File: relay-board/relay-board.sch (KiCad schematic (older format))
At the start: 74 parts, among them IC1 LTV-357T, IC2 LTV-357T, IC3 LTV-357T, IC4 LTV-357T, IC5 LTV-357T, IC6 LTV-357T, IC7 LTV-357T, IC8 LTV-357T, K1 RELAY_JS5N-K, K10 CONN_3, K11 CONN_3, K12 CONN_3, K13 CONN_3, K14 CONN_3, K15 CONN_3, K16 CONN_3, K2 RELAY_JS5N-K, K3 RELAY_JS5N-K, K4 RELAY_JS5N-K, K5 RELAY_JS5N-K, K6 RELAY_JS5N-K, K7 RELAY_JS5N-K, K8 RELAY_JS5N-K, K9 CONN_3, P1 CONN_4, P2 CONN_4, P3 DIL6, P4 CONN_2, P5 CONN_2, Q1 BS107, Q2 BS107, Q3 BS107, Q4 BS107, Q5 BS107, Q6 BS107, Q7 BS107, Q8 BS107, U1 PCF8574

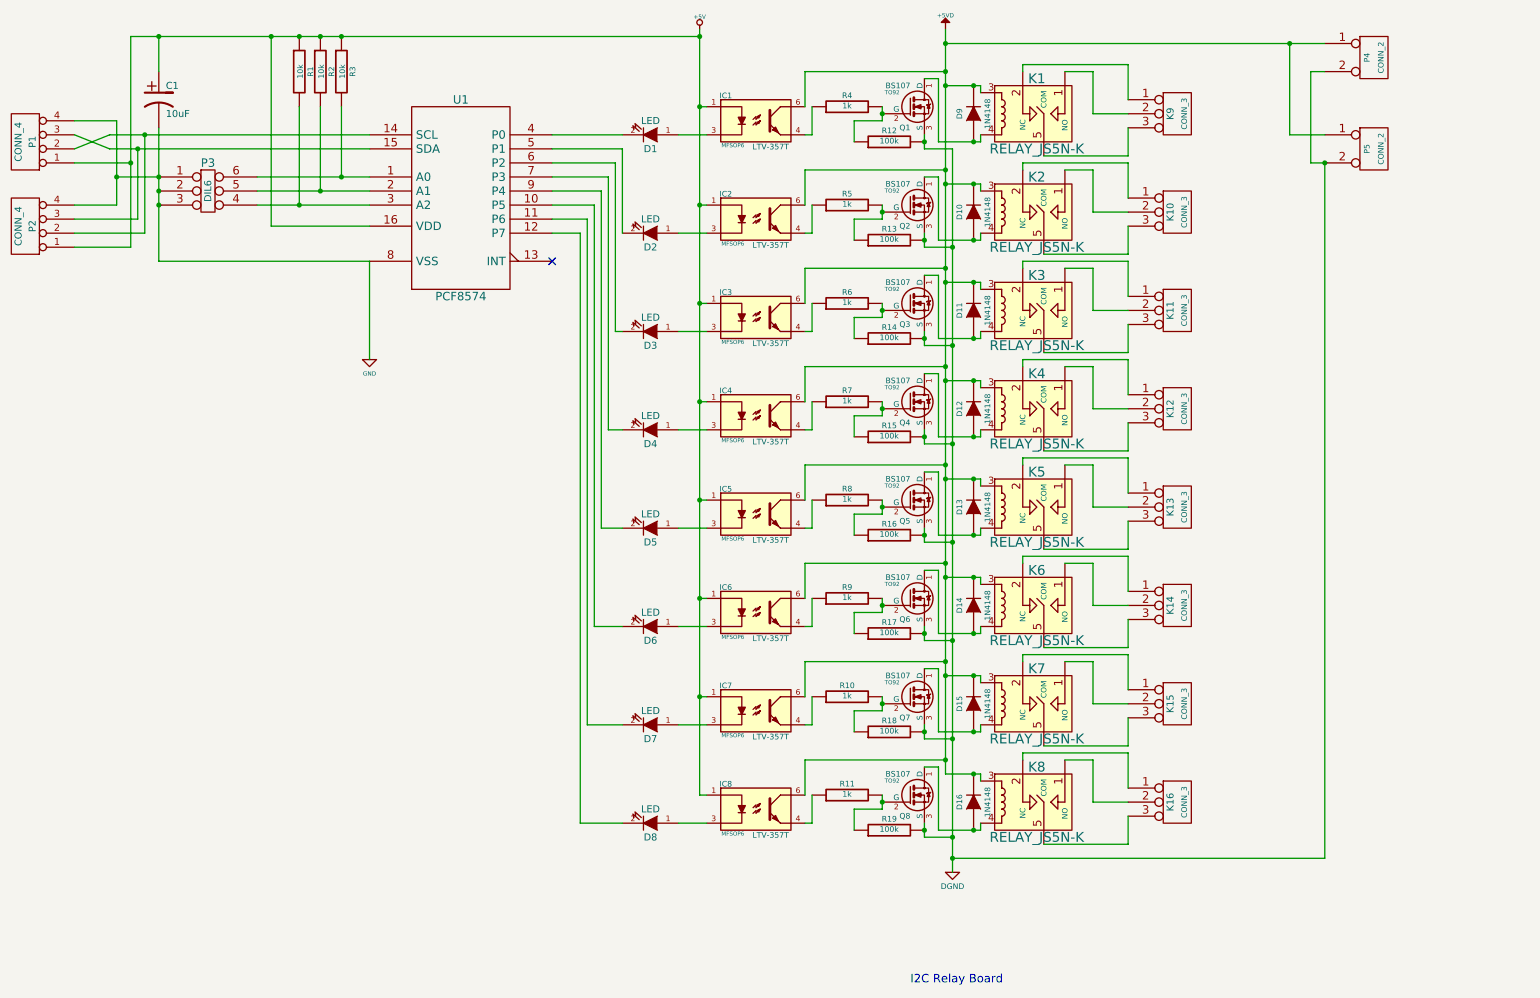
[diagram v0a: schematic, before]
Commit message: [relay-board] Updated schema, created PCB and added libraries with modules.
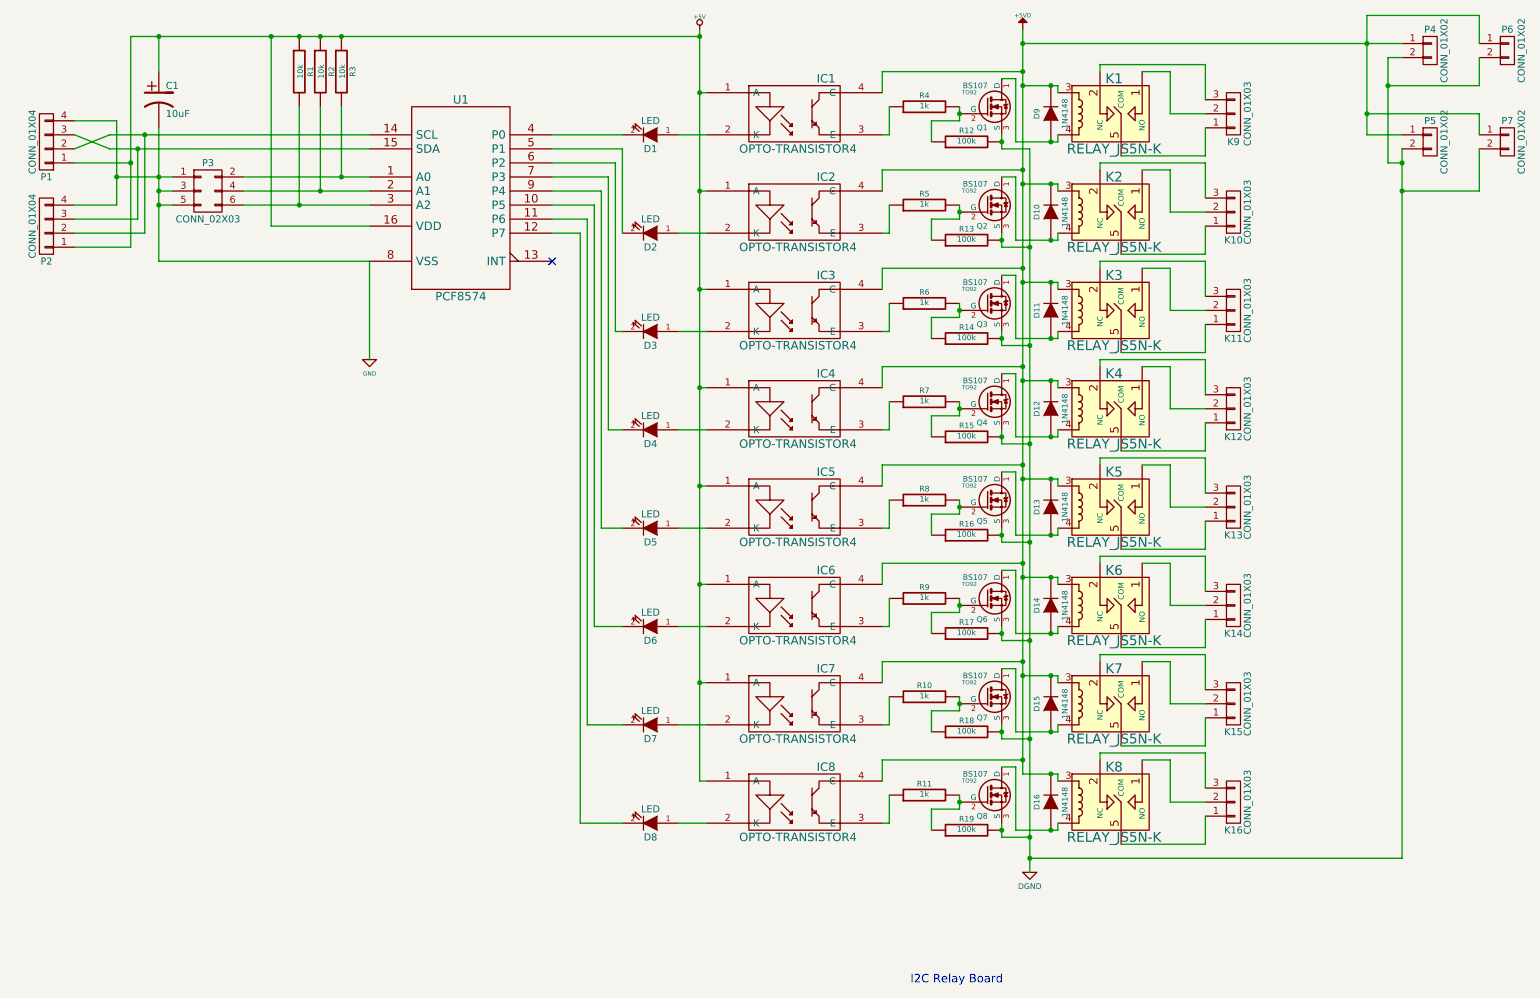
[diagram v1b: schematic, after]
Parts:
- removed IC1, IC2, IC3, IC4, IC5, IC6, IC7, IC8: LTV-357T, MFSOP6, symbol LTV-357T
- removed K10, K11, K12, K13, K14, K15, K16, K9: CONN_3, ~, symbol CONN_3
- removed P1, P2: CONN_4, ~, symbol CONN_4
- removed P3: DIL6, ~, symbol DIL6
- removed P4, P5: CONN_2, ~, symbol CONN_2
- added IC1, IC2, IC3, IC4, IC5, IC6, IC7, IC8: OPTO-TRANSISTOR4, symbol OPTO-TRANSISTOR4
- added K10, K11, K12, K13, K14, K15, K16, K9: CONN_01X03, symbol CONN_01X03
- added P1, P2: CONN_01X04, symbol CONN_01X04
- added P3: CONN_02X03, symbol CONN_02X03
- added P4, P5, P6, P7: CONN_01X02, symbol CONN_01X02
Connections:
- net +5V: now also IC1.1 (A), IC2.1 (A), IC3.1 (A), IC4.1 (A), IC5.1 (A), IC6.1 (A), IC7.1 (A), IC8.1 (A), P1.1 (P1), P2.1 (P1)
- net +5VD: now also IC1.4 (C), IC2.4 (C), IC3.4 (C), IC4.4 (C), IC5.4 (C), IC6.4 (C), IC7.4 (C), IC8.4 (C), P4.1 (P1), P5.1 (P1), P6.1 (P1), P7.1 (P1)
- net DGND: now also P4.2 (P2), P5.2 (P2), P6.2 (P2), P7.2 (P2)
- net GND: now also P1.4 (P4), P2.4 (P4), P3.1 (P1), P3.3 (P3), P3.5 (P5)
- net at R3.2, U1.1 (A0): now also P3.2 (P2)
- net at U1.14 (SCL): now also P1.2 (P2), P2.2 (P2)
- net at U1.15 (SDA): now also P1.3 (P3), P2.3 (P3)
- net at R2.2, U1.2 (A1): now also P3.4 (P4)
- net at R1.2, U1.3 (A2): now also P3.6 (P6)
- net at D1.1 (A): now also IC1.2 (K)
- net at D2.1 (A): now also IC2.2 (K)
- net at D3.1 (A): now also IC3.2 (K)
- net at D4.1 (A): now also IC4.2 (K)
- net at D5.1 (A): now also IC5.2 (K)
- net at D6.1 (A): now also IC6.2 (K)
- net at D7.1 (A): now also IC7.2 (K)
- net at D8.1 (A): now also IC8.2 (K)
- net at R4.1: now also IC1.3 (E)
- net at R5.1: now also IC2.3 (E)
- net at R6.1: now also IC3.3 (E)
- net at R7.1: now also IC4.3 (E)
- net at R8.1: now also IC5.3 (E)
- net at R9.1: now also IC6.3 (E)
- net at R10.1: now also IC7.3 (E)
- net at R11.1: now also IC8.3 (E)
- net at K1.1 (NO): now also K9.2 (P2)
- net at K1.2 (NC): now also K9.3 (P3)
- net at K1.5 (COM): now also K9.1 (P1)
- net at K2.1 (NO): now also K10.2 (P2)
- net at K2.2 (NC): now also K10.3 (P3)
- net at K2.5 (COM): now also K10.1 (P1)
- net at K3.1 (NO): now also K11.2 (P2)
- net at K3.2 (NC): now also K11.3 (P3)
- net at K3.5 (COM): now also K11.1 (P1)
- net at K4.1 (NO): now also K12.2 (P2)
- net at K4.2 (NC): now also K12.3 (P3)
- net at K4.5 (COM): now also K12.1 (P1)
- net at K5.1 (NO): now also K13.2 (P2)
- net at K5.2 (NC): now also K13.3 (P3)
- net at K5.5 (COM): now also K13.1 (P1)
- net at K6.1 (NO): now also K14.2 (P2)
- net at K6.2 (NC): now also K14.3 (P3)
- net at K6.5 (COM): now also K14.1 (P1)
- net at K7.1 (NO): now also K15.2 (P2)
- net at K7.2 (NC): now also K15.3 (P3)
- net at K7.5 (COM): now also K15.1 (P1)
- net at K8.1 (NO): now also K16.2 (P2)
- net at K8.2 (NC): now also K16.3 (P3)
- net at K8.5 (COM): now also K16.1 (P1)
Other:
- moved on the sheet: D10, D11, D12, D13, D14, D15, D16, D9, K1, K2, K3, K4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

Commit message: [relay-board] Updated PCB.
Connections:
- net at K1.1 (NO): now also K9.3 (P3); no longer K9.2 (P2)
- net at K1.2 (NC): now also K9.2 (P2); no longer K9.3 (P3)
- net at K2.1 (NO): now also K10.3 (P3); no longer K10.2 (P2)
- net at K2.2 (NC): now also K10.2 (P2); no longer K10.3 (P3)
- net at K3.1 (NO): now also K11.3 (P3); no longer K11.2 (P2)
- net at K3.2 (NC): now also K11.2 (P2); no longer K11.3 (P3)
- net at K4.1 (NO): now also K12.3 (P3); no longer K12.2 (P2)
- net at K4.2 (NC): now also K12.2 (P2); no longer K12.3 (P3)
- net at K5.1 (NO): now also K13.3 (P3); no longer K13.2 (P2)
- net at K5.2 (NC): now also K13.2 (P2); no longer K13.3 (P3)
- net at K6.1 (NO): now also K14.3 (P3); no longer K14.2 (P2)
- net at K6.2 (NC): now also K14.2 (P2); no longer K14.3 (P3)
- net at K7.1 (NO): now also K15.3 (P3); no longer K15.2 (P2)
- net at K7.2 (NC): now also K15.2 (P2); no longer K15.3 (P3)
- net at K8.1 (NO): now also K16.3 (P3); no longer K16.2 (P2)
- net at K8.2 (NC): now also K16.2 (P2); no longer K16.3 (P3)
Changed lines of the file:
@@
 LIBS:contrib
 LIBS:valves
-LIBS:i2c
 LIBS:philips
 LIBS:relay-board-cache
@@
 Sheet 1 1
 Title ""
-Date "12 apr 2015"
+Date "13 may 2015"
 Rev ""
 Comp ""
@@
 Wire Wire Line
 	8700 5900 8700 5950
-Wire Wire Line
-	9450 5900 8700 5900
-Wire Wire Line
-	9450 6150 9450 5900
-Wire Wire Line
-	9200 6250 9450 6250
-Wire Wire Line
-	9200 5950 9200 6250
-Wire Wire Line
-	9000 5950 9200 5950
 Connection ~ 7700 5550
 Wire Wire Line
@@
 Wire Wire Line
 	8700 5200 8700 5250
-Wire Wire Line
-	9450 5200 8700 5200
-Wire Wire Line
-	9450 5450 9450 5200
-Wire Wire Line
-	9200 5550 9450 5550
-Wire Wire Line
-	9200 5250 9200 5550
-Wire Wire Line
-	9000 5250 9200 5250
 Connection ~ 7700 4850
 Wire Wire Line
@@
 Wire Wire Line
 	8700 4500 8700 4550
-Wire Wire Line
-	9450 4500 8700 4500
-Wire Wire Line
-	9450 4750 9450 4500
-Wire Wire Line
-	9200 4850 9450 4850
-Wire Wire Line
-	9200 4550 9200 4850
-Wire Wire Line
-	9000 4550 9200 4550
 Connection ~ 7700 4150
 Wire Wire Line
@@
 Wire Wire Line
 	8700 3800 8700 3850
-Wire Wire Line
-	9450 3800 8700 3800
-Wire Wire Line
-	9450 4050 9450 3800
-Wire Wire Line
-	9200 4150 9450 4150
-Wire Wire Line
-	9200 3850 9200 4150
-Wire Wire Line
-	9000 3850 9200 3850
 Connection ~ 7700 3450
 Wire Wire Line
@@
 Wire Wire Line
 	8700 3100 8700 3150
-Wire Wire Line
-	9450 3100 8700 3100
-Wire Wire Line
-	9450 3350 9450 3100
-Wire Wire Line
-	9200 3450 9450 3450
-Wire Wire Line
-	9200 3150 9200 3450
-Wire Wire Line
-	9000 3150 9200 3150
 Connection ~ 7700 2750
 Wire Wire Line
@@
 Wire Wire Line
 	8700 2400 8700 2450
-Wire Wire Line
-	9450 2400 8700 2400
-Wire Wire Line
-	9450 2650 9450 2400
-Wire Wire Line
-	9200 2750 9450 2750
-Wire Wire Line
-	9200 2450 9200 2750
-Wire Wire Line
-	9000 2450 9200 2450
 Connection ~ 7700 2050
 Wire Wire Line
@@
 Wire Wire Line
 	8700 1700 8700 1750
-Wire Wire Line
-	9450 1700 8700 1700
-Wire Wire Line
-	9450 1950 9450 1700
-Wire Wire Line
-	9200 2050 9450 2050
-Wire Wire Line
-	9200 1750 9200 2050
-Wire Wire Line
-	9000 1750 9200 1750
 Connection ~ 7700 1350
 Wire Wire Line
@@
 Wire Wire Line
 	8700 1000 8700 1050
-Wire Wire Line
-	9450 1000 8700 1000
-Wire Wire Line
-	9450 1250 9450 1000
-Wire Wire Line
-	9200 1350 9450 1350
-Wire Wire Line
-	9200 1050 9200 1350
-Wire Wire Line
-	9000 1050 9200 1050
 Wire Wire Line
 	5900 1500 5700 1500
@@
 	1    0    0    -1
 $EndComp
+Wire Wire Line
+	9000 1050 9450 1050
+Wire Wire Line
+	9450 1050 9450 1250
+Wire Wire Line
+	9450 1350 9300 1350
+Wire Wire Line
+	9300 1350 9300 1000
+Wire Wire Line
+	9300 1000 8700 1000
+Wire Wire Line
+	9000 1750 9450 1750
+Wire Wire Line
+	9450 1750 9450 1950
+Wire Wire Line
+	8700 1700 9300 1700
+Wire Wire Line
+	9300 1700 9300 2050
+Wire Wire Line
+	9300 2050 9450 2050
+Wire Wire Line
+	9000 2450 9450 2450
+Wire Wire Line
+	9450 2450 9450 2650
+Wire Wire Line
+	8700 2400 9300 2400
+Wire Wire Line
+	9300 2400 9300 2750
+Wire Wire Line
+	9300 2750 9450 2750
+Wire Wire Line
+	9000 3150 9450 3150
+Wire Wire Line
+	9450 3150 9450 3350
+Wire Wire Line
+	8700 3100 9300 3100
+Wire Wire Line
+	9300 3100 9300 3450
+Wire Wire Line
+	9300 3450 9450 3450
+Wire Wire Line
+	9000 3850 9450 3850
+Wire Wire Line
+	9450 3850 9450 4050
+Wire Wire Line
+	8700 3800 9300 3800
+Wire Wire Line
+	9300 3800 9300 4150
+Wire Wire Line
+	9300 4150 9450 4150
+Wire Wire Line
+	9000 5250 9450 5250
+Wire Wire Line
+	9450 5250 9450 5450
+Wire Wire Line
+	8700 5200 9300 5200
+Wire Wire Line
+	9300 5200 9300 5550
+Wire Wire Line
+	9300 5550 9450 5550
+Wire Wire Line
+	9000 4550 9450 4550
+Wire Wire Line
+	9450 4550 9450 4750
+Wire Wire Line
+	8700 4500 9300 4500
+Wire Wire Line
+	9300 4500 9300 4850
+Wire Wire Line
+	9300 4850 9450 4850
+Wire Wire Line
+	9000 5950 9450 5950
+Wire Wire Line
+	9450 5950 9450 6150
+Wire Wire Line
+	8700 5900 9300 5900
+Wire Wire Line
+	9300 5900 9300 6250
+Wire Wire Line
+	9300 6250 9450 6250
 $EndSCHEMATC
